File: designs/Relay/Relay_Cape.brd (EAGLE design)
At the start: 71.8 x 58.4 mm, 51 parts, among them T1 3904, T2 3904, T3 3904, T4 3904, X1 RELAY_SINGLE_POLE_DOUBLE_THROW, X2 RELAY_SINGLE_POLE_DOUBLE_THROW, X3 RELAY_SINGLE_POLE_DOUBLE_THROW, X4 RELAY_SINGLE_POLE_DOUBLE_THROW

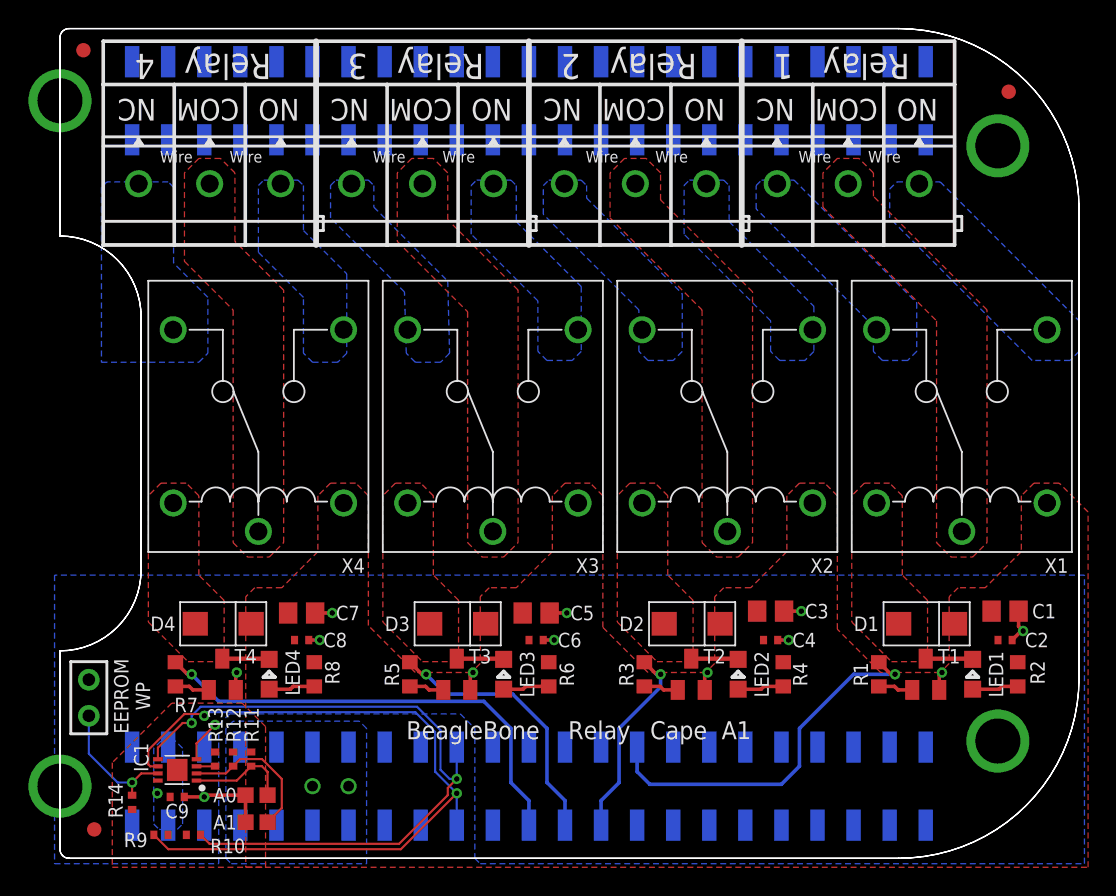
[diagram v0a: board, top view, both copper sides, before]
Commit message: Added the revised EAGLE schematics. Also removed two files that were probably not intended to be added as they are lock files in EAGLE.
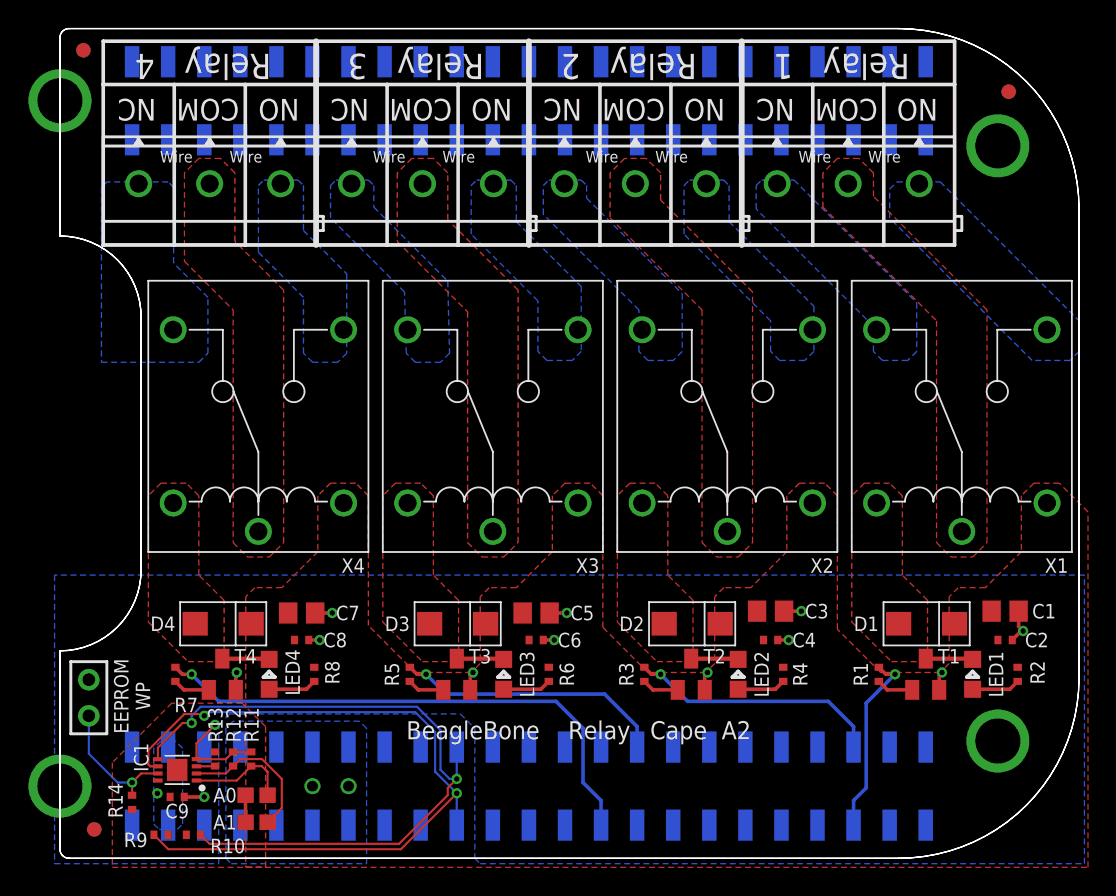
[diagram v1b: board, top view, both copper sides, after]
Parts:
- added FUD4, FUD5, FUD6: FIDUCIAL, GHI:FIDUCIAL_40MIL
- R1, R2, R3, R4, R5, R6, R7, R8: device GHI-BasicComponents:0603 -> GHI-BasicComponents:0402
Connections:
- net GND: now also R11.1, R12.1; no longer SJ1.1, SJ2.1
- net RELAY1: now also BB.CAPE1.B9.41; no longer BB.CAPE1.B9.30
- net RELAY2: now also BB.CAPE1.B9.42; no longer BB.CAPE1.B9.27
- net RELAY3: now also BB.CAPE1.B9.30; no longer BB.CAPE1.B9.25
- net RELAY4: now also BB.CAPE1.B9.27; no longer BB.CAPE1.B9.23
- net VCC: now also SJ1.1, SJ2.1; no longer R11.1, R12.1
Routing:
- net RELAY1: track 26.5 -> 13.2 mm
- net RELAY4: track 32.9 -> 37.8 mm
- net RELAY2: track 13.9 -> 17.9 mm
- net VCC: track 0.00 -> 1.91 mm
- net GND: track 22.9 -> 22.3 mm
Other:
- board text added: "A2"
